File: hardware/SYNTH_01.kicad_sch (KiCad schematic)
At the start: 0 parts

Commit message: adding U1 to hardware
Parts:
- added C1: 100nF, symbol Device:C
- added J1: RPI4_GPIO_40, symbol Connector_Generic:Conn_02x20_Odd_Even
- added U1: MCP23017-E/SP, Package_DIP:DIP-28_W7.62mm, symbol Interface_Expansion:MCP23017x-x-SP
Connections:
- new net +3V3: J1.1 (Pin_1), U1.9 (V_{DD})
- new net GND: J1.6 (Pin_6), U1.10 (V_{SS})
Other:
- note added: "U1 est un expandeur rajoutant 16 GPIO au raspberry pi. Ils communiquent tous les deux via le language I2C"
- note added: "envoi le courant vers le reste du circuit"
- note added: "fonctionnement du bus"
- note added: "la masse le retour du courant donc GND"
- note added: "les 16 prises GPIO"
- note added: "reçoit le ground du circuit"
- note added: "vdd signifie arrivée du courant positif"

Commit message: linking 3v3 and GND to C1 (condensateur de découplage)
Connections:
- net +3V3: now also C1.1
- net GND: now also C1.2
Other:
- moved on the sheet: C1
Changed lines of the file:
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@@
 	(symbol
 		(lib_id "Device:C")
-		(at 88.9 54.61 0)
+		(at 78.74 85.09 0)
 		(unit 1)
 		(body_style 1)
@@
 		(fields_autoplaced yes)
 		(property "Reference" "C1"
-			(at 92.71 53.3399 0)
+			(at 82.55 83.8199 0)
 			(show_name no)
 			(do_not_autoplace no)
@@
 		)
 		(property "Value" "100nF"
-			(at 92.71 55.8799 0)
+			(at 82.55 86.3599 0)
 			(show_name no)
 			(do_not_autoplace no)
@@
 		)
 		(property "Footprint" ""
-			(at 89.8652 58.42 0)
-			(hide yes)
-			(show_name no)
-			(do_not_autoplace no)
-			(effects
-				(font
-					(size 1.27 1.27)
-				)
-			)
-		)
-		(property "Datasheet" ""
-			(at 88.9 54.61 0)
+			(at 79.7052 88.9 0)
+			(hide yes)
+			(show_name no)
+			(do_not_autoplace no)
+			(effects
+				(font
+					(size 1.27 1.27)
+				)
+			)
+		)
+		(property "Datasheet" ""
+			(at 78.74 85.09 0)
 			(hide yes)
 			(show_name no)
@@
 		)
 		(property "Description" "Unpolarized capacitor"
-			(at 88.9 54.61 0)
+			(at 78.74 85.09 0)
 			(hide yes)
 			(show_name no)
@@
 				(path "/8736209f-7c7b-4c76-92ee-96040748110a"
 					(reference "C1")
+					(unit 1)
+				)
+			)
+		)
+	)
+	(symbol
+		(lib_id "power:+3V3")
+		(at 78.74 81.28 0)
+		(unit 1)
+		(body_style 1)
+		(exclude_from_sim no)
+		(in_bom yes)
+		(on_board yes)
+		(in_pos_files yes)
+		(dnp no)
+		(fields_autoplaced yes)
+		(property "Reference" "#PWR05"
+			(at 78.74 85.09 0)
+			(hide yes)
+			(show_name no)
+			(do_not_autoplace no)
+			(effects
+				(font
+					(size 1.27 1.27)
+				)
+			)
+		)
+		(property "Value" "+3V3"
+			(at 78.74 76.2 0)
+			(show_name no)
+			(do_not_autoplace no)
+			(effects
+				(font
+					(size 1.27 1.27)
+				)
+			)
+		)
+		(property "Footprint" ""
+			(at 78.74 81.28 0)
+			(hide yes)
+			(show_name no)
+			(do_not_autoplace no)
+			(effects
+				(font
+					(size 1.27 1.27)
+				)
+			)
+		)
+		(property "Datasheet" ""
+			(at 78.74 81.28 0)
+			(hide yes)
+			(show_name no)
+			(do_not_autoplace no)
+			(effects
+				(font
+					(size 1.27 1.27)
+				)
+			)
+		)
+		(property "Description" "Power symbol creates a global label with name \"+3V3\""
+			(at 78.74 81.28 0)
+			(hide yes)
+			(show_name no)
+			(do_not_autoplace no)
+			(effects
+				(font
+					(size 1.27 1.27)
+				)
+			)
+		)
+		(pin "1"
+		)
+		(instances
+			(project "SYNTH_01"
+				(path "/8736209f-7c7b-4c76-92ee-96040748110a"
+					(reference "#PWR05")
 					(unit 1)
 				)
@@
 					(unit 1)
 				)
+			)
+		)
+	)
+	(symbol
+		(lib_id "power:GND")
+		(at 78.74 88.9 0)
+		(unit 1)
+		(body_style 1)
+		(exclude_from_sim no)
+		(in_bom yes)
+		(on_board yes)
+		(in_pos_files yes)
+		(dnp no)
+		(fields_autoplaced yes)
+		(property "Reference" "#PWR06"
+			(at 78.74 95.25 0)
+			(hide yes)
+			(show_name no)
+			(do_not_autoplace no)
+			(effects
+				(font
+					(size 1.27 1.27)
+				)
+			)
+		)
+		(property "Value" "GND"
+			(at 78.74 93.98 0)
+			(show_name no)
+			(do_not_autoplace no)
+			(effects
+				(font
+					(size 1.27 1.27)
+				)
+			)
+		)
+		(property "Footprint" ""
+			(at 78.74 88.9 0)
+			(hide yes)
+			(show_name no)
+			(do_not_autoplace no)
+			(effects
+				(font
+					(size 1.27 1.27)
+				)
+			)
+		)
+		(property "Datasheet" ""
+			(at 78.74 88.9 0)
+			(hide yes)
+			(show_name no)
+			(do_not_autoplace no)
+			(effects
+				(font
+					(size 1.27 1.27)
+				)
+			)
+		)
+		(property "Description" "Power symbol creates a global label with name \"GND\" , ground"
+			(at 78.74 88.9 0)
+			(hide yes)
+			(show_name no)
+			(do_not_autoplace no)
+			(effects
+				(font
+					(size 1.27 1.27)
+				)
+			)
+		)
+		(pin "1"
+		)
+		(instances
+			(project "SYNTH_01"
+				(path "/8736209f-7c7b-4c76-92ee-96040748110a"
+					(reference "#PWR06")
+					(unit 1)
+				)

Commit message: fixed unlined labels
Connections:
- net GND: now also U1.15 (A0), U1.16 (A1), U1.17 (A2)
- net SCL: now also J1.5 (Pin_5), U1.12 (SCK)
- net SDA: now also J1.3 (Pin_3), U1.13 (SDA)
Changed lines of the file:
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@@
+	(wire
+		(pts
+			(xy 86.36 105.41) (xy 91.44 105.41)
+		)
+		(stroke
+			(width 0)
+			(type default)
+		)
+	)
+	(wire
+		(pts
+			(xy 86.36 69.85) (xy 91.44 69.85)
+		)
+		(stroke
+			(width 0)
+			(type default)
+		)
+	)
+	(wire
+		(pts
+			(xy 35.56 69.85) (xy 40.64 69.85)
+		)
+		(stroke
+			(width 0)
+			(type default)
+		)
+	)
 	(wire
 		(pts
@@
 	(wire
 		(pts
+			(xy 86.36 102.87) (xy 91.44 102.87)
+		)
+		(stroke
+			(width 0)
+			(type default)
+		)
+	)
+	(wire
+		(pts
+			(xy 86.36 107.95) (xy 91.44 107.95)
+		)
+		(stroke
+			(width 0)
+			(type default)
+		)
+	)
+	(wire
+		(pts
+			(xy 35.56 67.31) (xy 40.64 67.31)
+		)
+		(stroke
+			(width 0)
+			(type default)
+		)
+	)
+	(wire
+		(pts
 			(xy 53.34 69.85) (xy 57.15 69.85)
 		)
@@
 		)
 		(stroke
+			(width 0)
+			(type default)
+		)
+	)
+	(wire
+		(pts
+			(xy 86.36 67.31) (xy 91.44 67.31)
+		)
+		(stroke

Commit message: adding resistor between reset and +3v3
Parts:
- added R1: 10k, symbol Device:R
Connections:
- net +3V3: now also R1.1
- net at U1.18 (~{RESET}): now also R1.2
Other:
- moved on the sheet: C1
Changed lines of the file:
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@@
+	(wire
+		(pts
+			(xy 82.55 95.25) (xy 91.44 95.25)
+		)
+		(stroke
+			(width 0)
+			(type default)
+		)
+	)
 	(wire
 		(pts
 			(xy 35.56 67.31) (xy 40.64 67.31)
+		)
+		(stroke
+			(width 0)
+			(type default)
+		)
+	)
+	(wire
+		(pts
+			(xy 91.44 95.25) (xy 91.44 90.17)
 		)
 		(stroke
@@
 	)
 	(symbol
+		(lib_id "Device:R")
+		(at 82.55 91.44 0)
+		(unit 1)
+		(body_style 1)
+		(exclude_from_sim no)
+		(in_bom yes)
+		(on_board yes)
+		(in_pos_files yes)
+		(dnp no)
+		(fields_autoplaced yes)
+		(property "Reference" "R1"
+			(at 85.09 90.1699 0)
+			(show_name no)
+			(do_not_autoplace no)
+			(effects
+				(font
+					(size 1.27 1.27)
+				)
+				(justify left)
+			)
+		)
+		(property "Value" "10k"
+			(at 85.09 92.7099 0)
+			(show_name no)
+			(do_not_autoplace no)
+			(effects
+				(font
+					(size 1.27 1.27)
+				)
+				(justify left)
+			)
+		)
+		(property "Footprint" ""
+			(at 80.772 91.44 90)
+			(hide yes)
+			(show_name no)
+			(do_not_autoplace no)
+			(effects
+				(font
+					(size 1.27 1.27)
+				)
+			)
+		)
+		(property "Datasheet" ""
+			(at 82.55 91.44 0)
+			(hide yes)
+			(show_name no)
+			(do_not_autoplace no)
+			(effects
+				(font
+					(size 1.27 1.27)
+				)
+			)
+		)
+		(property "Description" "Resistor"
+			(at 82.55 91.44 0)
+			(hide yes)
+			(show_name no)
+			(do_not_autoplace no)
+			(effects
+				(font
+					(size 1.27 1.27)
+				)
+			)
+		)
+		(pin "2"
+		)
+		(pin "1"
+		)
+		(instances
+			(project "SYNTH_01"
+				(path "/8736209f-7c7b-4c76-92ee-96040748110a"
+					(reference "R1")
+					(unit 1)
+				)
+			)
+		)
+	)
+	(symbol
 		(lib_id "Device:C")
-		(at 78.74 85.09 0)
+		(at 90.17 53.34 0)
 		(unit 1)
 		(body_style 1)
@@
 		(fields_autoplaced yes)
 		(property "Reference" "C1"
-			(at 82.55 83.8199 0)
+			(at 93.98 52.0699 0)
 			(show_name no)
 			(do_not_autoplace no)
@@
 		)
 		(property "Value" "100nF"
-			(at 82.55 86.3599 0)
+			(at 93.98 54.6099 0)
 			(show_name no)
 			(do_not_autoplace no)
@@
 		)
 		(property "Footprint" ""
-			(at 79.7052 88.9 0)
+			(at 91.1352 57.15 0)
 			(hide yes)
 			(show_name no)
@@
 		)
 		(property "Datasheet" ""
-			(at 78.74 85.09 0)
+			(at 90.17 53.34 0)
 			(hide yes)
 			(show_name no)
@@
 		)
 		(property "Description" "Unpolarized capacitor"
-			(at 78.74 85.09 0)
+			(at 90.17 53.34 0)
 			(hide yes)
 			(show_name no)
@@
 	(symbol
 		(lib_id "power:+3V3")
-		(at 78.74 81.28 0)
+		(at 90.17 49.53 0)
 		(unit 1)
 		(body_style 1)
@@
 		(fields_autoplaced yes)
 		(property "Reference" "#PWR05"
-			(at 78.74 85.09 0)
+			(at 90.17 53.34 0)
 			(hide yes)
 			(show_name no)
@@
 		)
 		(property "Value" "+3V3"
-			(at 78.74 76.2 0)
+			(at 90.17 44.45 0)
 			(show_name no)
 			(do_not_autoplace no)
@@
 		)
 		(property "Footprint" ""
-			(at 78.74 81.28 0)
+			(at 90.17 49.53 0)
 			(hide yes)
 			(show_name no)
@@
 		)
 		(property "Datasheet" ""
-			(at 78.74 81.28 0)
+			(at 90.17 49.53 0)
 			(hide yes)
 			(show_name no)
@@
 		)
 		(property "Description" "Power symbol creates a global label with name \"+3V3\""
-			(at 78.74 81.28 0)
+			(at 90.17 49.53 0)
 			(hide yes)
 			(show_name no)
@@
 	)
 	(symbol
+		(lib_id "power:+3V3")
+		(at 82.55 87.63 0)
+		(unit 1)
+		(body_style 1)
+		(exclude_from_sim no)
+		(in_bom yes)
+		(on_board yes)
+		(in_pos_files yes)
+		(dnp no)
+		(property "Reference" "#PWR07"
+			(at 82.55 91.44 0)
+			(hide yes)
+			(show_name no)
+			(do_not_autoplace no)
+			(effects
+				(font
+					(size 1.27 1.27)
+				)
+			)
+		)
+		(property "Value" "+3V3"
+			(at 96.52 60.96 0)
+			(show_name no)
+			(do_not_autoplace no)
+			(effects
+				(font
+					(size 1.27 1.27)
+				)
+			)
+		)
+		(property "Footprint" ""
+			(at 82.55 87.63 0)
+			(hide yes)
+			(show_name no)
+			(do_not_autoplace no)
+			(effects
+				(font
+					(size 1.27 1.27)
+				)
+			)
+		)
+		(property "Datasheet" ""
+			(at 82.55 87.63 0)
+			(hide yes)
+			(show_name no)
+			(do_not_autoplace no)
+			(effects
+				(font
+					(size 1.27 1.27)
+				)
+			)
+		)
+		(property "Description" "Power symbol creates a global label with name \"+3V3\""
+			(at 82.55 87.63 0)
+			(hide yes)
+			(show_name no)
+			(do_not_autoplace no)
+			(effects
+				(font
+					(size 1.27 1.27)
+				)
+			)
+		)
+		(pin "1"
+		)
+		(instances
+			(project "SYNTH_01"
+				(path "/8736209f-7c7b-4c76-92ee-96040748110a"
+					(reference "#PWR07")
+					(unit 1)
+				)
+			)
+		)
+	)
+	(symbol
 		(lib_id "power:GND")
-		(at 78.74 88.9 0)
+		(at 90.17 57.15 0)
 		(unit 1)
 		(body_style 1)
@@
 		(fields_autoplaced yes)
 		(property "Reference" "#PWR06"
-			(at 78.74 95.25 0)
+			(at 90.17 63.5 0)
 			(hide yes)
 			(show_name no)
@@
 		)
 		(property "Value" "GND"
-			(at 78.74 93.98 0)
+			(at 90.17 62.23 0)
 			(show_name no)
 			(do_not_autoplace no)
@@
 		)
 		(property "Footprint" ""
-			(at 78.74 88.9 0)
+			(at 90.17 57.15 0)
 			(hide yes)
 			(show_name no)
@@
 		)
 		(property "Datasheet" ""
-			(at 78.74 88.9 0)
+			(at 90.17 57.15 0)
 			(hide yes)
 			(show_name no)
@@
 		)
 		(property "Description" "Power symbol creates a global label with name \"GND\" , ground"
-			(at 78.74 88.9 0)
-			(hide yes)
-			(show_name no)
+			(at 90.17 57.15 0)
+			(hide yes)
+			(show_name no)

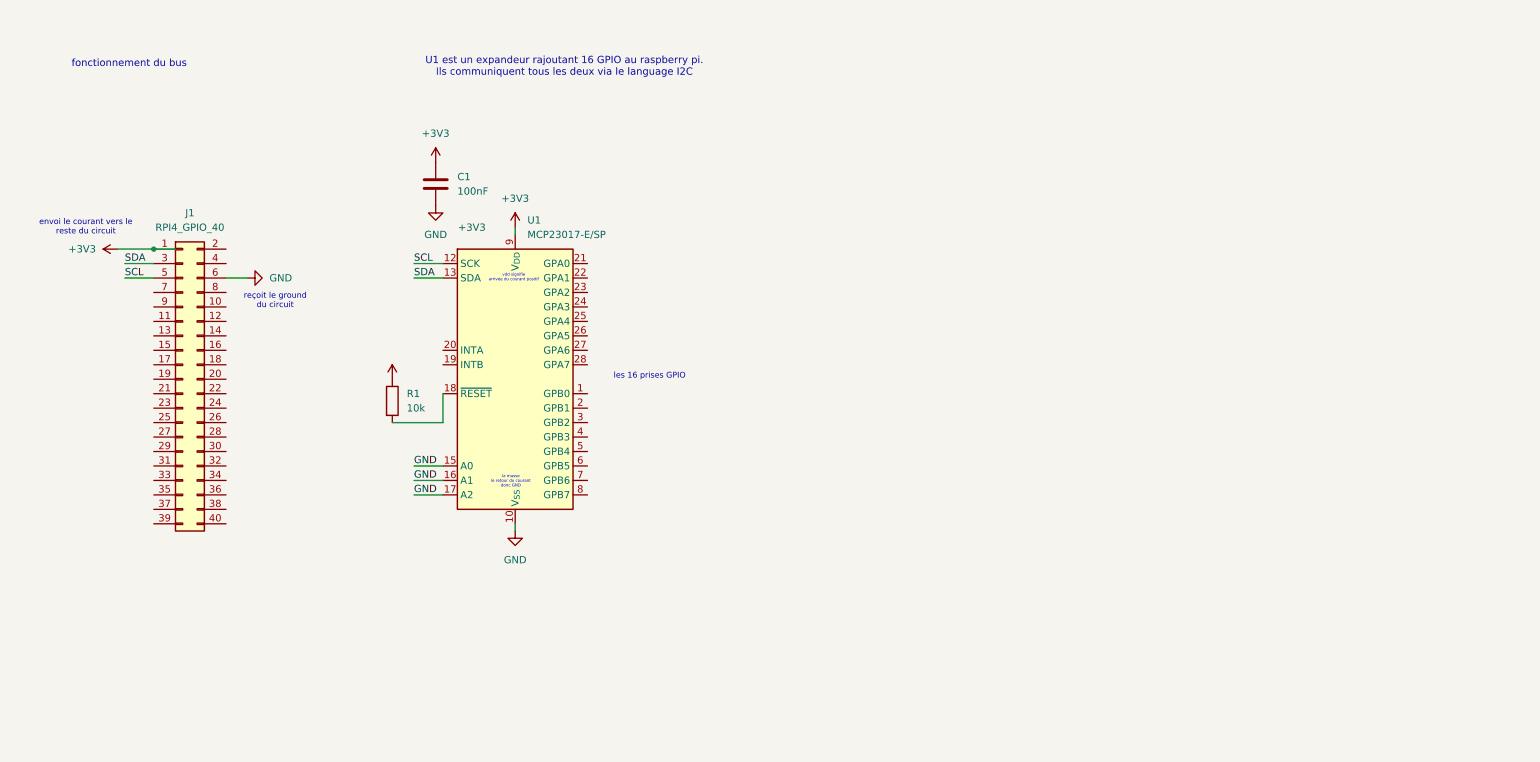
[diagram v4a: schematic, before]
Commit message: adding SWITCH:SW_push
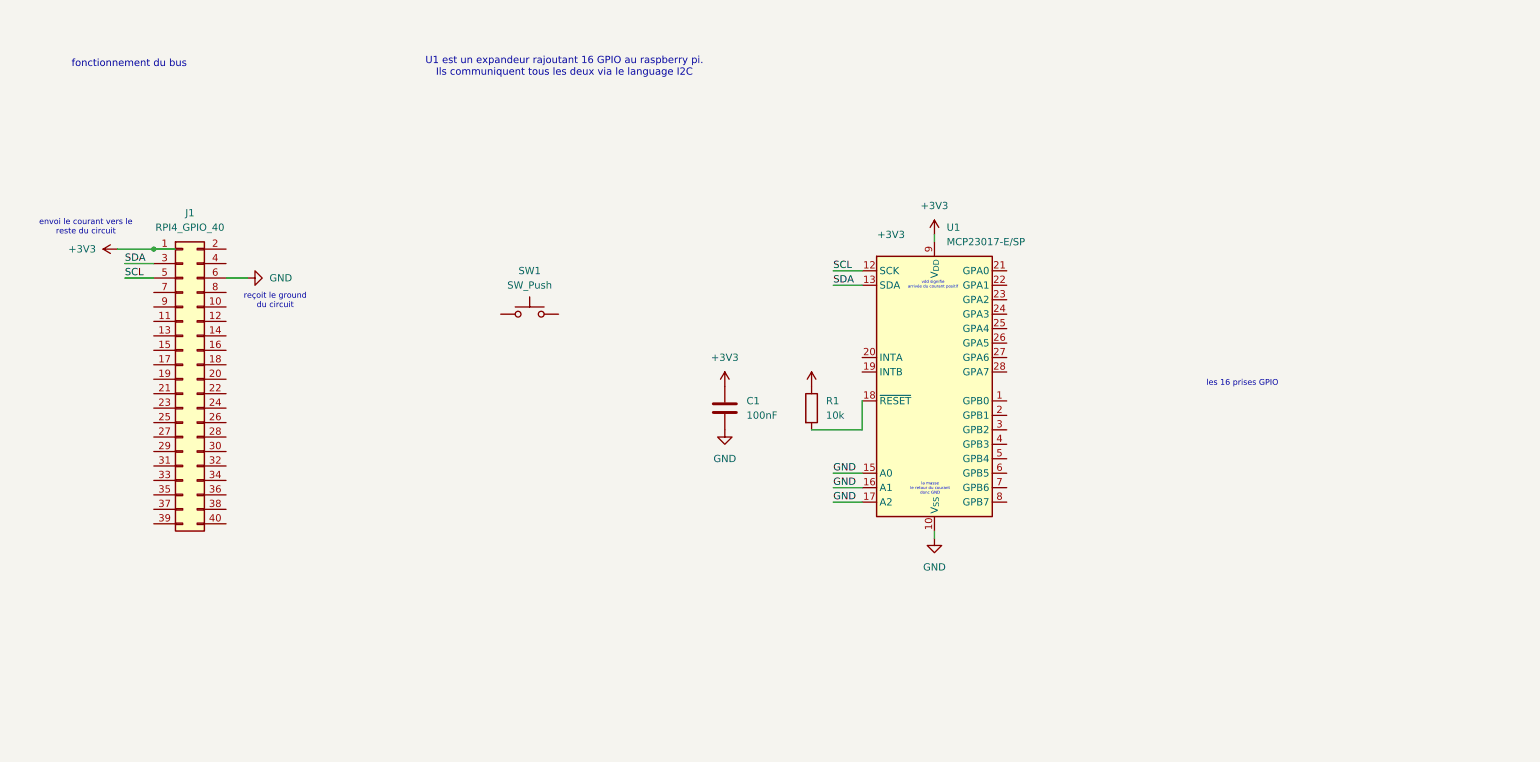
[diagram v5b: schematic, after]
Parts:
- added SW1: SW_Push, symbol Switch:SW_Push
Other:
- moved on the sheet: C1, R1, U1

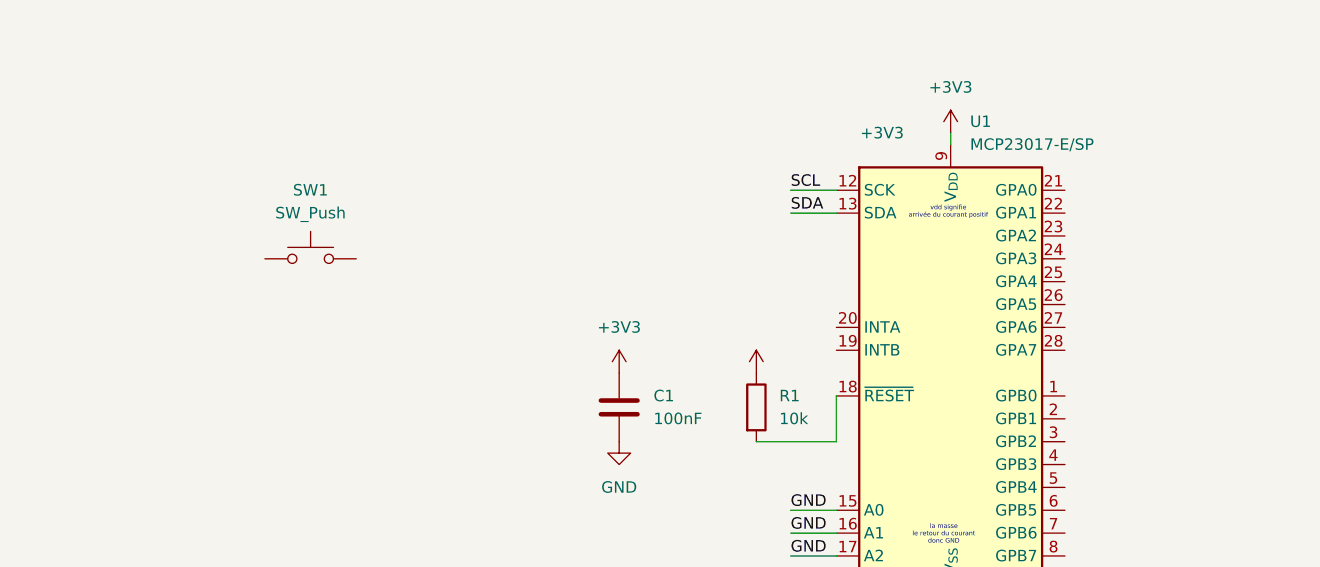
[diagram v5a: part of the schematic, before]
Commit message: [PCB] adding ROW and COL logic and linking to U1
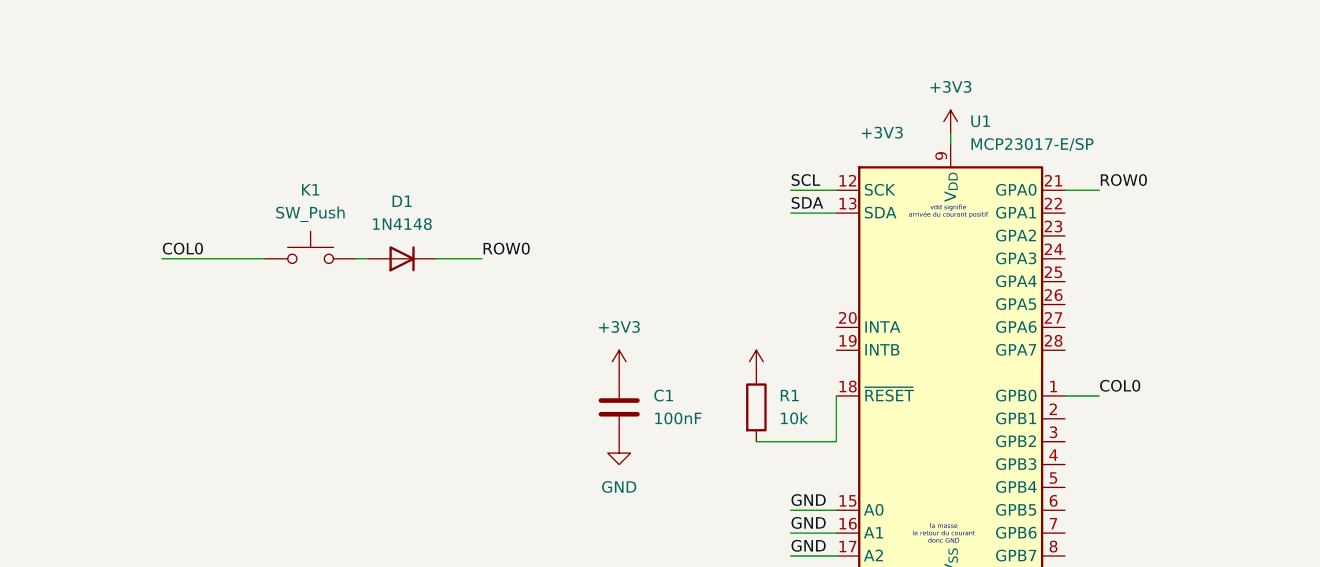
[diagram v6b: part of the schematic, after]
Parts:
- added D1: 1N4148, symbol Device:D
- renumbered SW1 to K1
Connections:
- net COL0: now reaches K1.1
- net COL0: now also U1.1 (GPB0)
- net at K1.2: now also D1.2 (A)
- net ROW0: now reaches U1.21 (GPA0)
- net ROW0: now also D1.1 (K)
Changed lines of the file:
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@@
+	(wire
+		(pts
+			(xy 90.17 76.2) (xy 101.6 76.2)
+		)
+		(stroke
+			(width 0)
+			(type default)
+		)
+	)
 	(wire
 		(pts
@@
 	(wire
 		(pts
+			(xy 190.5 91.44) (xy 194.31 91.44)
+		)
+		(stroke
+			(width 0)
+			(type default)
+		)
+	)
+	(wire
+		(pts
 			(xy 156.21 96.52) (xy 165.1 96.52)
 		)
@@
 	(wire
 		(pts
+			(xy 113.03 76.2) (xy 111.76 76.2)
+		)
+		(stroke
+			(width 0)
+			(type default)
+		)
+	)
+	(wire
+		(pts
 			(xy 160.02 68.58) (xy 165.1 68.58)
 		)
@@
 		(pts
 			(xy 34.29 64.77) (xy 40.64 64.77)
+		)
+		(stroke
+			(width 0)
+			(type default)
+		)
+	)
+	(wire
+		(pts
+			(xy 120.65 76.2) (xy 125.73 76.2)
+		)
+		(stroke
+			(width 0)
+			(type default)
+		)
+	)
+	(wire
+		(pts
+			(xy 190.5 68.58) (xy 194.31 68.58)
 		)
 		(stroke
@@
 		)
 	)
+	(label "COL0"
+		(at 90.17 76.2 0)
+		(effects
+			(font
+				(size 1.27 1.27)
+			)
+			(justify left bottom)
+		)
+	)
+	(label "ROW0"
+		(at 194.31 68.58 0)
+		(effects
+			(font
+				(size 1.27 1.27)
+			)
+			(justify left bottom)
+		)
+	)
+	(label "ROW0"
+		(at 125.73 76.2 0)
+		(effects
+			(font
+				(size 1.27 1.27)
+			)
+			(justify left bottom)
+		)
+	)
+	(label "COL0"
+		(at 194.31 91.44 0)
+		(effects
+			(font
+				(size 1.27 1.27)
+			)
+			(justify left bottom)
+		)
+	)
 	(label "SDA"
 		(at 160.02 71.12 0)
@@
 	)
 	(symbol
+		(lib_id "Device:D")
+		(at 116.84 76.2 180)
+		(unit 1)
+		(body_style 1)
+		(exclude_from_sim no)
+		(in_bom yes)
+		(on_board yes)
+		(in_pos_files yes)
+		(dnp no)
+		(fields_autoplaced yes)
+		(property "Reference" "D1"
+			(at 116.84 69.85 0)
+			(show_name no)
+			(do_not_autoplace no)
+			(effects
+				(font
+					(size 1.27 1.27)
+				)
+			)
+		)
+		(property "Value" "1N4148"
+			(at 116.84 72.39 0)
+			(show_name no)
+			(do_not_autoplace no)
+			(effects
+				(font
+					(size 1.27 1.27)
+				)
+			)
+		)
+		(property "Footprint" ""
+			(at 116.84 76.2 0)
+			(hide yes)
+			(show_name no)
+			(do_not_autoplace no)
+			(effects
+				(font
+					(size 1.27 1.27)
+				)
+			)
+		)
+		(property "Datasheet" ""
+			(at 116.84 76.2 0)
+			(hide yes)
+			(show_name no)
+			(do_not_autoplace no)
+			(effects
+				(font
+					(size 1.27 1.27)
+				)
+			)
+		)
+		(property "Description" "Diode"
+			(at 116.84 76.2 0)
+			(hide yes)
+			(show_name no)
+			(do_not_autoplace no)
+			(effects
+				(font
+					(size 1.27 1.27)
+				)
+			)
+		)
+		(property "Sim.Device" "D"
+			(at 116.84 76.2 0)
+			(hide yes)
+			(show_name no)
+			(do_not_autoplace no)
+			(effects
+				(font
+					(size 1.27 1.27)
+				)
+			)
+		)
+		(property "Sim.Pins" "1=K 2=A"
+			(at 116.84 76.2 0)
+			(hide yes)
+			(show_name no)
+			(do_not_autoplace no)
+			(effects
+				(font
+					(size 1.27 1.27)
+				)
+			)
+		)
+		(pin "2"
+		)
+		(pin "1"
+		)
+		(instances
+			(project "SYNTH_01"
+				(path "/8736209f-7c7b-4c76-92ee-96040748110a"
+					(reference "D1")
+					(unit 1)
+				)
+			)
+		)
+	)
+	(symbol
 		(lib_id "power:GND")
 		(at 140.97 96.52 0)
@@
 		(dnp no)
 		(fields_autoplaced yes)
-		(property "Reference" "SW1"
+		(property "Reference" "K1"
 			(at 106.68 68.58 0)
 			(show_name no)
@@
 			(project "SYNTH_01"
 				(path "/8736209f-7c7b-4c76-92ee-96040748110a"
-					(reference "SW1")
+					(reference "K1")
 					(unit 1)
 				)
